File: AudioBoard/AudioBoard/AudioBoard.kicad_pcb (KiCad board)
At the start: 4 copper layers, 250 x 160 mm, 270 parts, among them J1 IN, J2 XLR_L, J3 FX_RETURN, J4 FX_SEND, J5 INS_OUT, J6 XLR_R, J7 Barrel_Jack, J8 NMJ6HFD2, J9 NMJ6HFD2, SW2 SW_SPDT_321, SW3 PWR_SW, U10 TL072, U11 TL072, U14 TL072, U15 NJM4556A, U16 TL072, U17 TL072, U18 NJM4556A, U19 TL072, U2 NE5532, U20 TL072, U4 TL072, U5 TL072, U6 TL072, U7 TL072, U8 TL072, U9 TL072

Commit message: optimized codec layout
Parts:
- added REF**: MountingHole_2.2mm_M2, MountingHole:MountingHole_2.2mm_M2, F.Cu at (54.0, 95.0)
- added REF**: MountingHole_2.2mm_M2, MountingHole:MountingHole_2.2mm_M2, F.Cu at (296.0, 205.0)
- added REF**: MountingHole_2.2mm_M2, MountingHole:MountingHole_2.2mm_M2, F.Cu at (54.0, 205.0)
- added REF**: MountingHole_2.2mm_M2, MountingHole:MountingHole_2.2mm_M2, F.Cu at (296.0, 95.0)
- moved C108 42.0 mm to (238.0, 99.7)
- moved C109 42.0 mm to (241.2, 99.7)
- moved C110 42.0 mm to (237.8, 96.4)
- moved C111 42.0 mm to (242.5, 96.4)
- moved C112 42.0 mm to (233.8, 90.9)
- moved R59 42.0 mm to (238.8, 102.0)
- moved R60 42.0 mm to (240.4, 102.0)
- moved R61 42.0 mm to (235.4, 97.2)
- moved R62 42.0 mm to (242.5, 98.0)
- moved R63 42.0 mm to (237.9, 98.0)
- moved C37 42.0 mm to (235.6, 89.3)
- moved C38 42.0 mm to (242.6, 94.3)
- moved R64 42.0 mm to (240.2, 97.1)
- moved R65 42.0 mm to (235.6, 93.1)
- moved U4 42.0 mm to (239.2, 91.8)
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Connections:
- C112 pad 2: /Audio_IO_conn/SEND_2 -> /Audio_IO_conn/OUT_L
- C117 pad 2: /Audio_IO_conn/SEND_1 -> /Audio_IO_conn/OUT_R
- C122 pad 2: /Audio_IO_conn/OUT_R -> /Audio_IO_conn/SEND_1
- C127 pad 2: /Audio_IO_conn/OUT_L -> /Audio_IO_conn/SEND_2
- R118 pad 1: /Audio_IO_conn/HEADPHONE_L -> /HeadphoneAmplifier1/OUT
- R120 pad 1: /Audio_IO_conn/HEADPHONE_L -> /HeadphoneAmplifier1/OUT
- R121 pad 1: /XLR_output_L/IN_N_P -> /XLR_output_L/IN_N_N
- R122 pad 1: /XLR_output_L/IN_N_N -> /XLR_output_L/IN_N_P
- R128 pad 1: /XLR_output_R/IN_N_P -> /XLR_output_R/IN_N_N
- R129 pad 1: /XLR_output_R/IN_N_N -> /XLR_output_R/IN_N_P
- U1 pad 10: /Instrument_output_L/IN_N -> /HeadphoneAmplifier/IN_P
- U1 pad 11: /Instrument_output_L/IN_P -> /HeadphoneAmplifier/IN_N
- U1 pad 12: /Instrument_output_R/IN_N -> /HeadphoneAmplifier1/IN_P
- U1 pad 13: /Instrument_output_R/IN_P -> /HeadphoneAmplifier1/IN_N
- U1 pad 36: /HeadphoneAmplifier/IN_N -> /Instrument_output_L/IN_N
- U1 pad 37: /HeadphoneAmplifier/IN_P -> /Instrument_output_L/IN_P
- U1 pad 38: /HeadphoneAmplifier1/IN_N -> /Instrument_output_R/IN_N
- U1 pad 39: /HeadphoneAmplifier1/IN_P -> /Instrument_output_R/IN_P
- U1 pad 40: /XLR_output_L/IN_N_N -> /Instrument_L1_send/IN_N
- U1 pad 41: /XLR_output_L/IN_N_P -> /Instrument_L1_send/IN_P
- U1 pad 42: /XLR_output_R/IN_N_N -> /Instrument_L2_send/IN_N
- U1 pad 43: /XLR_output_R/IN_N_P -> /Instrument_L2_send/IN_P
- U1 pad 6: /Instrument_L1_send/IN_N -> /XLR_output_R/IN_N_P
- U1 pad 7: /Instrument_L1_send/IN_P -> /XLR_output_R/IN_N_N
- U1 pad 8: /Instrument_L2_send/IN_N -> /XLR_output_L/IN_N_P
- U1 pad 9: /Instrument_L2_send/IN_P -> /XLR_output_L/IN_N_N
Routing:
- net /Instrument_L2_send/IN_N: track 83.5 -> 40.9 mm
- net /Instrument_L2_send/IN_P: track 82.6 -> 40.2 mm
- net /Instrument_output_L/IN_N: track 45.2 -> 67.2 mm
- net /Instrument_output_L/IN_P: track 44.4 -> 65.9 mm
- net /Instrument_L2_return/OUT_P: track 57.4 -> 38.3 mm, vias 2 -> 0
- net /Instrument_L1_send/IN_N: track 68.3 -> 49.3 mm, vias 2 -> 0
- net /Instrument_L1_send/IN_P: track 67.6 -> 49.1 mm, vias 2 -> 0
- net /Instrument_L1_return/OUT_P: track 51.3 -> 33.3 mm, vias 2 -> 0
- net /Instrument_L2_return/OUT_N: track 55.7 -> 38.3 mm, vias 2 -> 0
- net /Instrument_L1_return/OUT_N: track 49.9 -> 33.3 mm, vias 2 -> 0
- net /XLR_output_R/IN_N_P: track 43.4 -> 33.7 mm, vias 2 -> 0
- net /Instrument_Input/OUT_P: track 122.6 -> 114.4 mm, vias 0 -> 2
- net /XLR_output_L/IN_N_P: track 64.6 -> 57.8 mm, vias 2 -> 0
- net /XLR_output_R/IN_N_N: track 41.2 -> 34.4 mm, vias 2 -> 0
- net /Instrument_Input/OUT_N: track 120.9 -> 114.3 mm, vias 0 -> 2
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
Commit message: added power electronics
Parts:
- removed REF** (x4): MountingHole_2.2mm_M2, MountingHole:MountingHole_2.2mm_M2
- added C62: 100n, Capacitor_SMD:C_0402_1005Metric, F.Cu at (112.2, 170.5)
- added C81: 10uF tantal, Capacitor_Tantalum_SMD:CP_EIA-3216-18_Kemet-A, F.Cu at (108.0, 168.2)
- added C82: 47u, Capacitor_THT:CP_Radial_D6.3mm_P2.50mm, F.Cu at (99.9, 147.2)
- added C83: 47u, Capacitor_THT:CP_Radial_D6.3mm_P2.50mm, F.Cu at (99.9, 155.1)
- added C84: 47u, Capacitor_THT:CP_Radial_D6.3mm_P2.50mm, F.Cu at (99.9, 162.9)
- added C85: 100n, Capacitor_SMD:C_0402_1005Metric, F.Cu at (112.2, 172.5)
- added C86: 10uF tantal, Capacitor_Tantalum_SMD:CP_EIA-3216-18_Kemet-A, F.Cu at (108.0, 171.3)
- added C87: 47u, Capacitor_THT:CP_Radial_D6.3mm_P2.50mm, F.Cu at (99.9, 170.8)
- added FB1: GZ2012D601TF, Resistor_SMD:R_0805_2012Metric, F.Cu at (113.0, 168.1)
- added U12: AMS1117-3.3, Package_TO_SOT_SMD:SOT-223-3_TabPin2, F.Cu at (110.0, 147.5)
- added U13: AMS1117-3.3, Package_TO_SOT_SMD:SOT-223-3_TabPin2, F.Cu at (110.0, 155.8)
- added U3: TPS5430DDA, Package_SO:TI_SO-PowerPAD-8_ThermalVias, F.Cu at (109.4, 163.3)
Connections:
- net +48V renamed Phantom_PWR
- net /power/PhantomPower/+48V_EN_I renamed /power/PhantomPower/PP_EN_I

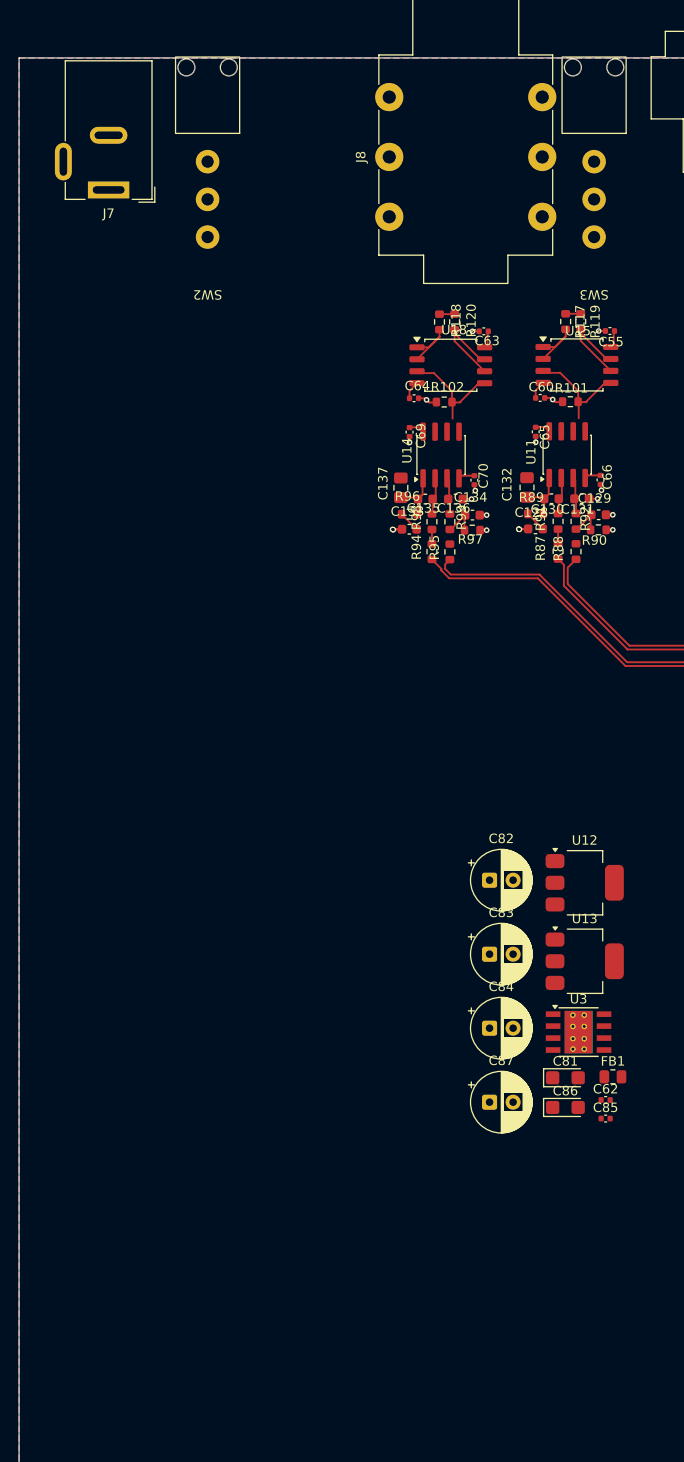
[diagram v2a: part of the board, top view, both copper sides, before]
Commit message: added power protection, dcdc modules
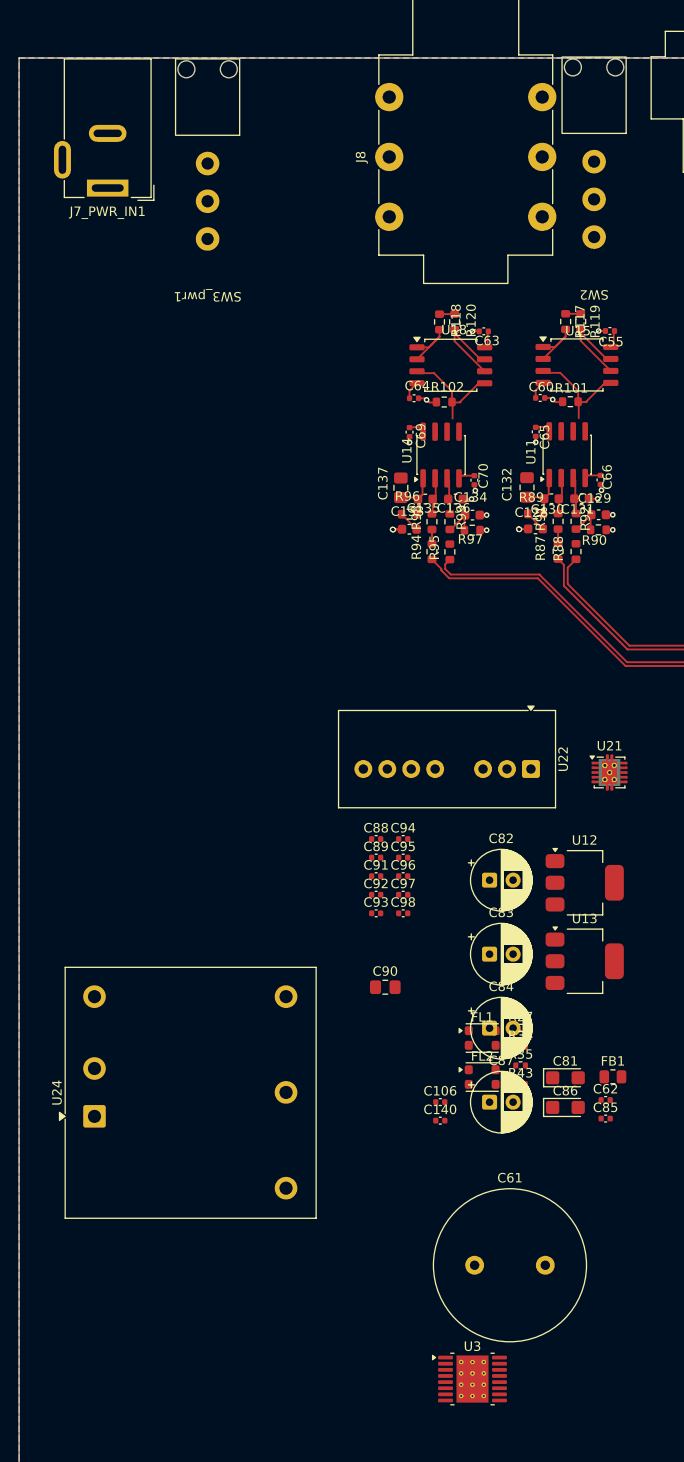
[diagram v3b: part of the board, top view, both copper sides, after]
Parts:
- removed J7: Barrel_Jack, Connector_BarrelJack:BarrelJack_Wuerth_6941xx301002
- removed SW3: PWR_SW, haoyu:SS-12D28G7
- added C106: 10uF, Capacitor_SMD:C_0402_1005Metric, F.Cu at (94.7, 170.8)
- added C140: 10uF, Capacitor_SMD:C_0402_1005Metric, F.Cu at (94.7, 172.7)
- added C61: 2200uF, Capacitor_THT:C_Radial_D16.0mm_H25.0mm_P7.50mm, F.Cu at (98.3, 188.1)
- added C88: 100n, Capacitor_SMD:C_0402_1005Metric, F.Cu at (87.9, 142.9)
- added C89: 100n, Capacitor_SMD:C_0402_1005Metric, F.Cu at (87.9, 144.8)
- added C90: 33nF, Capacitor_SMD:C_0805_2012Metric_Pad1.18x1.45mm_HandSolder, F.Cu at (88.8, 158.6)
- added C91: 10uF, Capacitor_SMD:C_0402_1005Metric, F.Cu at (87.9, 146.8)
- added C92: 10uF, Capacitor_SMD:C_0402_1005Metric, F.Cu at (87.9, 148.8)
- added C93: 10uF, Capacitor_SMD:C_0402_1005Metric, F.Cu at (87.9, 150.7)
- added C94: 10uF, Capacitor_SMD:C_0402_1005Metric, F.Cu at (90.8, 142.9)
- added C95: 10uF, Capacitor_SMD:C_0402_1005Metric, F.Cu at (90.8, 144.8)
- added C96: 10uF, Capacitor_SMD:C_0402_1005Metric, F.Cu at (90.8, 146.8)
- added C97: 100n, Capacitor_SMD:C_0402_1005Metric, F.Cu at (90.8, 148.8)
- added C98: 100n, Capacitor_SMD:C_0402_1005Metric, F.Cu at (90.8, 150.7)
- added FL1: ACT3225R510-W2, Inductor_SMD:L_CommonModeChoke_Coilank_ACM3225, F.Cu at (99.1, 164.0)
- added FL2: ACT3225R510-W2, Inductor_SMD:L_CommonModeChoke_Coilank_ACM3225, F.Cu at (99.1, 168.1)
- added J7_PWR_IN1: HC-DC-005-2.0T, Connector_BarrelJack:BarrelJack_Wuerth_6941xx301002, F.Cu at (59.4, 73.8)
- added R27: 0R, Resistor_SMD:R_0402_1005Metric, F.Cu at (103.2, 162.9)
- added R34: 0R, Resistor_SMD:R_0402_1005Metric, F.Cu at (103.2, 164.9)
- added R35: 0R, Resistor_SMD:R_0402_1005Metric, F.Cu at (103.2, 166.9)
- added R43: 0R, Resistor_SMD:R_0402_1005Metric, F.Cu at (103.2, 168.9)
- added SW3_pwr1: SS-12D28G7, haoyu:SS-12D28G7, F.Cu at (70.0, 84.8)
- added U21: TPS7A39, Package_SON:Texas_S-PVSON-N10_ThermalVias, F.Cu at (112.6, 135.8)
- added U22: URA2415S-6WR3, Converter_DCDC:Converter_DCDC_TRACO_TEC2-12xxWI_24xxWI_48xxWI_THT, F.Cu at (104.3, 135.4)
- added U24: TURB2405YMD-30WR3, Converter_DCDC:Converter_DCDC_TRACO_THL30-xxxxWI_THT, F.Cu at (58.0, 172.3)
- U3: value TPS5430DDA -> TPS26600PWP; footprint Package_SO:TI_SO-PowerPAD-8_ThermalVias -> Package_SO:HTSSOP-16-1EP_4.4x5mm_P0.65mm_EP3.4x5mm_Mask2.66x2.46mm_ThermalVias
- moved SW2 41.0 mm to (111.0, 84.6)
- moved U3 38.5 mm to (98.1, 200.1)
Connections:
- U3 pad 1: Net-(U3-BOOT) -> /power/input_pwr_protection/VIN
- U3 pad 2: unconnected-(U3-NC-Pad2) -> /power/input_pwr_protection/VIN
- U3 pad 3: unconnected-(U3-NC-Pad3) -> Net-(U3-MODE)
- U3 pad 4: Net-(U3-VSENSE) -> unconnected-(U3-NC-Pad4)
- U3 pad 5: unconnected-(U3-EN-Pad5) -> Net-(U3-MODE)
- U3 pad 6: GND -> Net-(U3-MODE)
- U3 pad 7: /power/AnalogPower/VIN -> /power/input_pwr_protection/\SHDN
- U3 pad 8: Net-(U3-PH) -> Net-(U3-MODE)
- U3 pad 9: GND -> GNDPWR

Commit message: assigned footprint to elements lcsc parts
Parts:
- added C100: 10uF, Capacitor_SMD:C_0402_1005Metric, F.Cu at (83.3, 199.7)
- added C101: 2200uF, Capacitor_THT:C_Radial_D16.0mm_H25.0mm_P7.50mm, F.Cu at (69.3, 200.5)
- added C99: 100n, Capacitor_SMD:C_0402_1005Metric, F.Cu at (83.3, 197.7)
- added FB2: BLM18PG121SN1D, Fuse:Fuse_0603_1608Metric, F.Cu at (83.9, 193.0)
- added FB3: BLM18PG121SN1D, Fuse:Fuse_0603_1608Metric, F.Cu at (83.9, 195.5)
- moved C61 9.56 mm to (107.7, 190.2)
- moved U3 9.56 mm to (107.4, 202.3)
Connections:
- J7_PWR_IN1 pad 1: GND -> GNDPWR
- U24 pad 1: /power/AnalogPower/VIN -> Net-(U24-+Vin)
- U24 pad 3: /power/+5V -> Net-(U24-+Vout)
- U3 pad 14: /power/AnalogPower/EN -> Net-(U3-~{FLT})
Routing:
- net GNDPWR: track 0.00 -> 95.2 mm
